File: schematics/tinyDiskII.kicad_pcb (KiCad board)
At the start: 2 copper layers, 95.3 x 50.8 mm, 51 parts, among them J2 SD_Card, J3 USB_B_Mini, J4 APPLEII_DISK_CONNECTOR, J5 Ext, SW1 RotaryEncoder_Switch, U1 MX25R3235FM1xx0, U10 AP1117-33, U2 SN74LVC244, U3 CH340C, U5 74LS125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

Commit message: [schematics] Removed old tracks, rewire in progress
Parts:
- added R15: 10k, Resistor_SMD:R_0805_2012Metric, F.Cu at (109.2, 101.2)
- D3, D4: value SD05_SOD323 -> -
- R2, R3, R4, R7: value R -> 10k
- R5, R6: value R -> 330
- U5: value 74LS125 -> 74AHCT125
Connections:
- C1 pad 1: Net-(C1-Pad1) -> +3V3
- J4 pad 13: /+12 -> unconnected-(J4-Pad13)
- J4 pad 15: /+12 -> unconnected-(J4-Pad15)
- J4 pad 17: /+12 -> unconnected-(J4-Pad17)
- J4 pad 19: /+12 -> unconnected-(J4-Pad19)
- J4 pad 9: /-12 -> unconnected-(J4-Pad9)
- J5 pad 6: /PD3 -> /PA6
- J5 pad 7: /PD2 -> unconnected-(J5-Pad7)
- J5 pad 8: /PD1 -> unconnected-(J5-Pad8)
- U3 pad 16: Net-(C1-Pad1) -> +3V3
- U? pad 2: /LV_DISK_READ -> /PA6
- U? pad 21: /PD1 -> /LV_DISK_READ
- U? pad 22: /PD2 -> /SD_WP
- U? pad 23: /PD3 -> /SD_DETECT
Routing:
- net /LV_DISK_READ: track 25.4 -> 0.00 mm
- net /PD1: track 18.9 -> 0.00 mm, vias 1 -> 0
- net /PD3: track 18.1 -> 0.00 mm
- net /+12: track 17.2 -> 0.00 mm
- net /PD2: track 15.0 -> 0.00 mm, vias 1 -> 0
- net Net-(C1-Pad1): track 2.72 -> 0.00 mm
- net +3V3: track 191.5 -> 194.2 mm
- net unconnected-(J4-Pad9): track 0.00 -> 2.40 mm
- net /-12: track 2.40 -> 0.00 mm

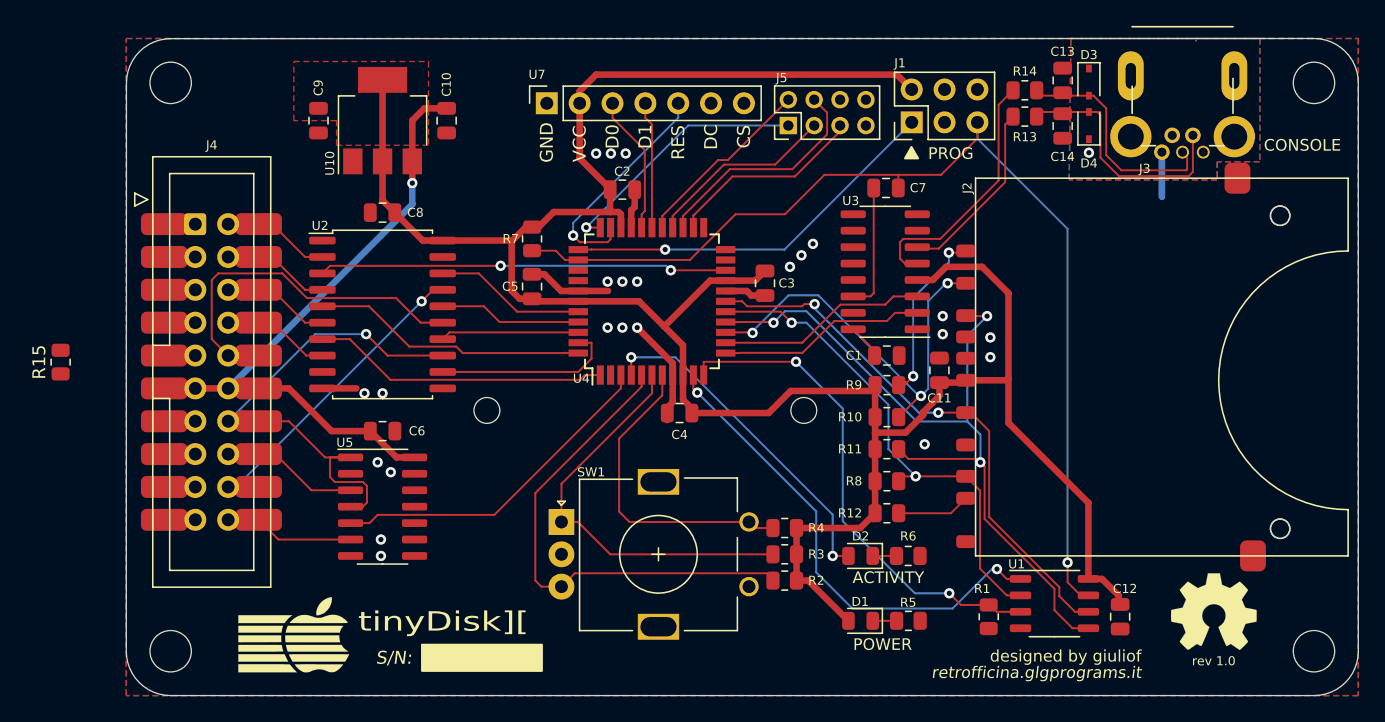
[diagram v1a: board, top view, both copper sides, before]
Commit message: [schematics] updated routing fixing errata of rev1.0
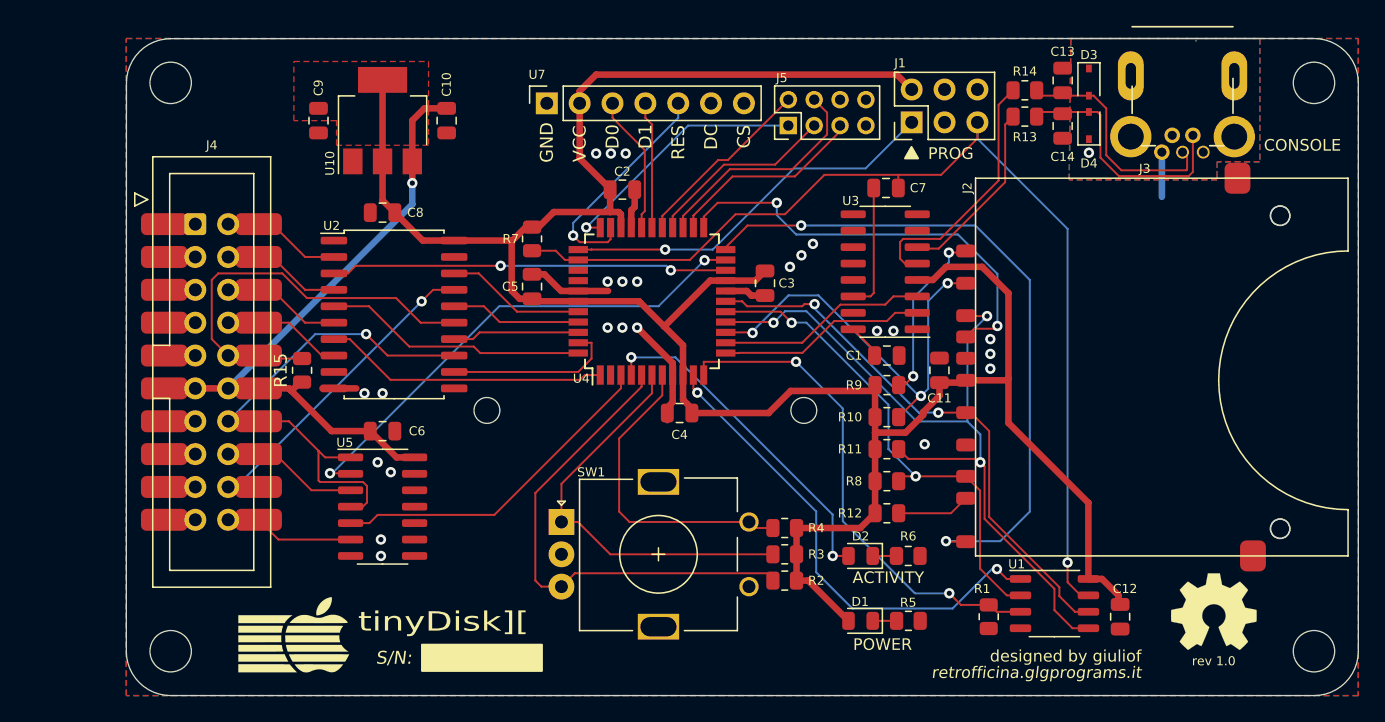
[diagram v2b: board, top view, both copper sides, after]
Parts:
- moved R15 18.7 mm to (127.9, 101.9)
- moved U2 0.89 mm to (135.0, 97.5)
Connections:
- J5 pad 6: /PA6 -> unconnected-(J5-Pad6)
- U? pad 2: /PA6 -> unconnected-(U4-Pad2)
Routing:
- net /SD_WP: track 0.00 -> 53.0 mm, vias 0 -> 2
- net /LV_DISK_READ: track 0.00 -> 39.0 mm, vias 0 -> 2
- net /SD_DETECT: track 0.00 -> 33.6 mm, vias 0 -> 2
- net /DISK_WRITE_EN: track 28.4 -> 31.8 mm
- net +5V: track 51.2 -> 52.3 mm
- net GND: vias 23 -> 24

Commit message: [schematics] rev1.1 label
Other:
- board text added: "rev 1.1"
- board text removed: "rev 1.0"
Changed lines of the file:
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@@
     (fp_line (start -3.9 -9.3) (end -3.9 -8.95) (layer "F.Fab") (width 0.127))
     (fp_line (start -3.91 -7.5606) (end -5.06 -7.5606) (layer "F.Fab") (width 0.1016))
-    (fp_arc (start 1.9725 -1.142) (mid 1.828618 -1.239695) (end 1.7649 -1.401498) (layer "F.Fab") (width 0.1016))
+    (fp_arc (start 1.9725 -1.142) (mid 1.828652 -1.239705) (end 1.7649 -1.401498) (layer "F.Fab") (width 0.1016))
     (fp_arc (start 2.7512 -1.4015) (mid 2.687459 -1.239703) (end 2.543601 -1.141999) (layer "F.Fab") (width 0.1016))
     (fp_arc (start 2.5436 -1.142) (mid 2.25805 -1.099197) (end 1.972501 -1.142) (layer "F.Fab") (width 0.1016))
@@
     (effects (font (size 0.9 0.9) (thickness 0.18)) (justify right))
   )
-  (gr_text "rev 1.0" (at 198.374 124.333) (layer "F.SilkS")
+  (gr_text "rev 1.1" (at 198.374 124.333) (layer "F.SilkS")
     (effects (font (size 0.7 0.7) (thickness 0.1)))
   )

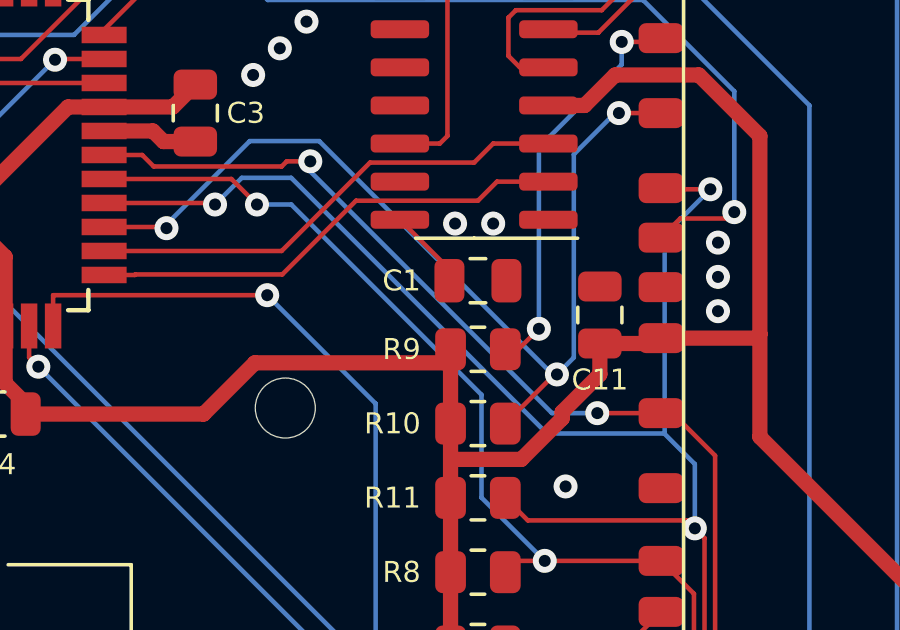
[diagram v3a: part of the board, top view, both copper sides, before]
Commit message: [schematics] Missing track, fixed
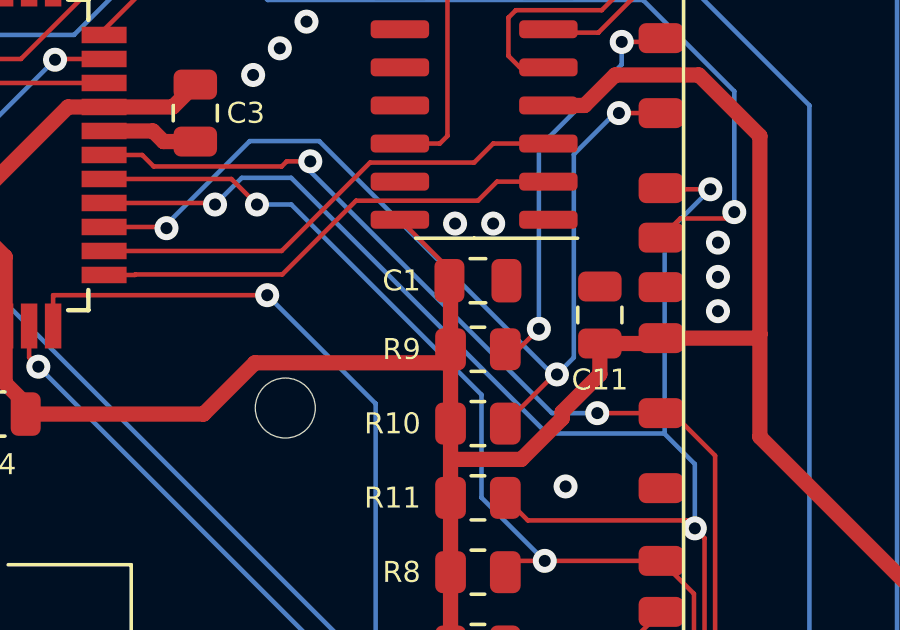
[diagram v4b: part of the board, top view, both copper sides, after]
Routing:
- net +3V3: track 194.2 -> 196.5 mm
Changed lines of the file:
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@@
     (fp_line (start -3.9 -9.3) (end -3.9 -8.95) (layer "F.Fab") (width 0.127))
     (fp_line (start -3.91 -7.5606) (end -5.06 -7.5606) (layer "F.Fab") (width 0.1016))
-    (fp_arc (start 1.9725 -1.142) (mid 1.828652 -1.239705) (end 1.7649 -1.401498) (layer "F.Fab") (width 0.1016))
+    (fp_arc (start 1.9725 -1.142) (mid 1.828646 -1.239707) (end 1.7649 -1.401498) (layer "F.Fab") (width 0.1016))
     (fp_arc (start 2.7512 -1.4015) (mid 2.687459 -1.239703) (end 2.543601 -1.141999) (layer "F.Fab") (width 0.1016))
     (fp_arc (start 2.5436 -1.142) (mid 2.25805 -1.099197) (end 1.972501 -1.142) (layer "F.Fab") (width 0.1016))
@@
   (segment (start 172.1885 107.95) (end 172.1885 110.4265) (width 0.508) (layer "F.Cu") (net 8))
   (segment (start 175.9072 105.3063) (end 174.5463 106.6672) (width 0.508) (layer "F.Cu") (net 8))
+  (segment (start 172.1885 100.7485) (end 172.151 100.711) (width 0.508) (layer "F.Cu") (net 8))
   (segment (start 177.165 102.804) (end 177.165 103.832752) (width 0.508) (layer "F.Cu") (net 8))
   (segment (start 144.714 96.327) (end 144.093711 95.706711) (width 0.508) (layer "F.Cu") (net 8))
@@
   (segment (start 137.221 91.821) (end 138.762 91.821) (width 0.508) (layer "F.Cu") (net 8))
   (segment (start 172.1885 105.4735) (end 172.1885 103.48) (width 0.508) (layer "F.Cu") (net 8))
+  (segment (start 172.1885 102.997) (end 172.1885 100.7485) (width 0.508) (layer "F.Cu") (net 8))
   (segment (start 146.177 90.7815) (end 147.3429 89.6156) (width 0.508) (layer "F.Cu") (net 8))
   (segment (start 191.008 119.253) (end 191.008 119.8832) (width 0.508) (layer "F.Cu") (net 8))
